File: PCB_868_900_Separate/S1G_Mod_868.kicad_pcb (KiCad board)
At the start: 4 copper layers, 60 x 33.3 mm, 79 parts, among them J2 20021121-00010C4LF, J5 0475890001-MicroUSBPort, P1 CONN_02X08, Q1 DMG2307L-7, SW1 CUS-12TB, SW2 B3U-1000P, T1 0732511150, T2 0732511150, U1 AP7361-33FGE-7, U2 ADF7023BCPZ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

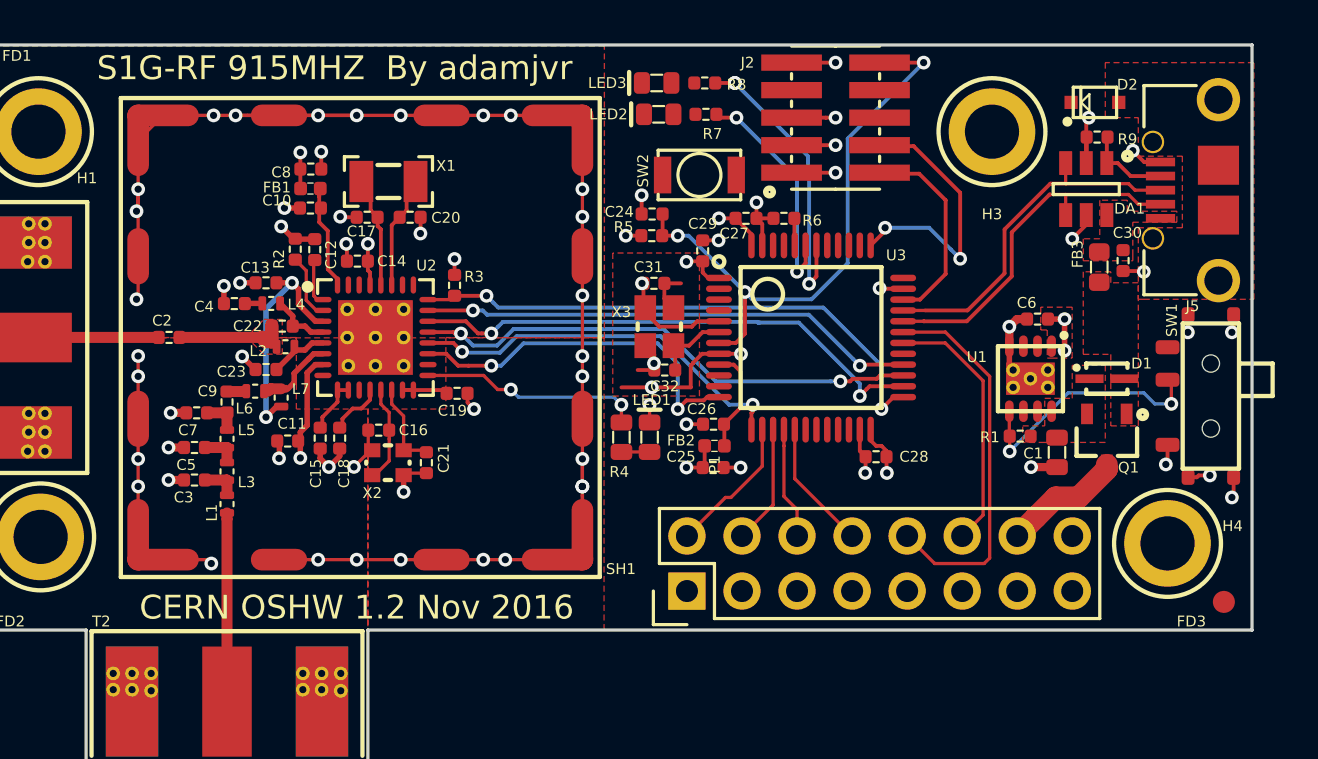
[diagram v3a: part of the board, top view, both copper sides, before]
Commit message: PCBs Tweaked A lot
PCBs have been tweaked. The separate implementation has been finished
but also has GPIOs from the MCU broken out to the connector, same for
the combined implementation. Both boards now have power indication LEDs
(red).
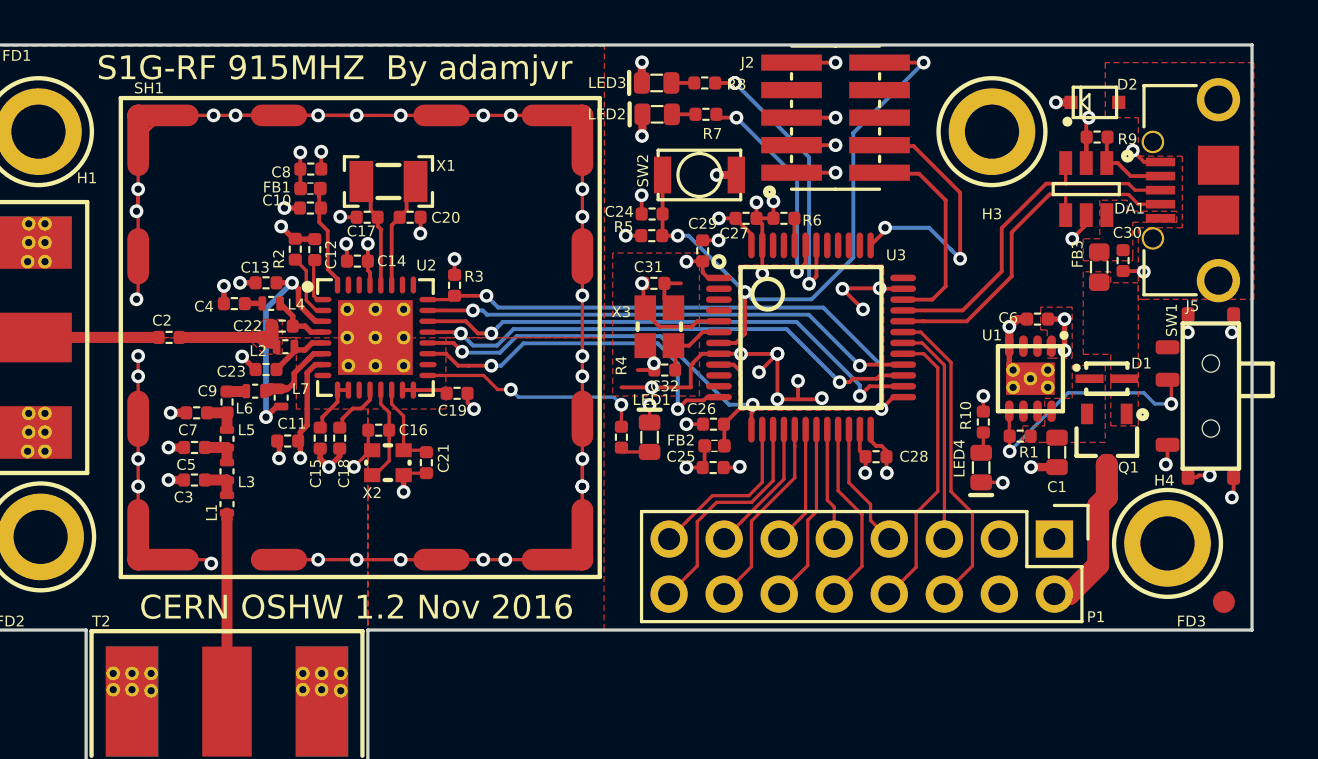
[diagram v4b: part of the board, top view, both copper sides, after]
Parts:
- added LED4: LTST-C193KRKT-5A, PCB_Footprints:LED0603, F.Cu at (104.0, 54.5)
- added R10: RC1005F102CS, PCB_Footprints:R0402, F.Cu at (104.1, 52.4)
- R4: value RC1608J202CS -> RC1005F102CS; footprint PCB_Footprints:R0603 -> PCB_Footprints:R0402
- moved P1 17.1 mm to (107.4, 57.8), turned to 270 degrees
- moved LED2 0.07 mm to (89.0, 38.2)
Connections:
- P1 pad 1: Net-(P1-Pad1) -> GND
- P1 pad 10: /MCU - STM32L052K8T6/USART1_RX -> /MCU - STM32L052K8T6/GPIO_PB10
- P1 pad 11: Net-(P1-Pad11) -> /MCU - STM32L052K8T6/GPIO_PB0
- P1 pad 12: /MCU - STM32L052K8T6/USART1_TX -> /MCU - STM32L052K8T6/GPIO_PB1
- P1 pad 13: Net-(P1-Pad13) -> /MCU - STM32L052K8T6/SPI2_MISO
- P1 pad 14: /PSU_IN -> /MCU - STM32L052K8T6/SPI2_MOSI
- P1 pad 15: GND -> /MCU - STM32L052K8T6/SPI2_NSS
- P1 pad 16: GND -> /MCU - STM32L052K8T6/SPI2_SCLK
- P1 pad 2: /MCU - STM32L052K8T6/SPI2_NSS -> /PSU_IN
- P1 pad 4: /MCU - STM32L052K8T6/SPI2_SCLK -> Net-(P1-Pad4)
- P1 pad 5: Net-(P1-Pad5) -> /MCU - STM32L052K8T6/USART1_TX
- P1 pad 6: /MCU - STM32L052K8T6/SPI2_MISO -> /MCU - STM32L052K8T6/USART1_RX
- P1 pad 7: Net-(P1-Pad7) -> /MCU - STM32L052K8T6/GPIO_PB11
- P1 pad 8: /MCU - STM32L052K8T6/SPI2_MOSI -> /MCU - STM32L052K8T6/GPIO_PA8
- P1 pad 9: Net-(P1-Pad9) -> /MCU - STM32L052K8T6/GPIO_PB2
- U3 pad 18: Net-(U3-Pad18) -> /MCU - STM32L052K8T6/GPIO_PB0
- U3 pad 19: Net-(U3-Pad19) -> /MCU - STM32L052K8T6/GPIO_PB1
- U3 pad 20: Net-(U3-Pad20) -> /MCU - STM32L052K8T6/GPIO_PB2
- U3 pad 21: Net-(U3-Pad21) -> /MCU - STM32L052K8T6/GPIO_PB10
- U3 pad 22: Net-(U3-Pad22) -> /MCU - STM32L052K8T6/GPIO_PB11
- U3 pad 29: Net-(U3-Pad29) -> /MCU - STM32L052K8T6/GPIO_PA8
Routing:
- net GND: track 141.9 -> 159.5 mm, vias 69 -> 84
- net /MCU - STM32L052K8T6/GPIO_PA8: track 0.00 -> 13.2 mm
- net /MCU - STM32L052K8T6/GPIO_PB10: track 0.00 -> 8.58 mm
- net /MCU - STM32L052K8T6/GPIO_PB1: track 0.00 -> 8.30 mm
- net /MCU - STM32L052K8T6/GPIO_PB11: track 0.00 -> 5.82 mm
- net /MCU - STM32L052K8T6/GPIO_PB0: track 0.00 -> 5.57 mm
- net /MCU - STM32L052K8T6/GPIO_PB2: track 0.00 -> 5.18 mm
- net /MCU - STM32L052K8T6/SPI2_SCLK: track 5.50 -> 10.5 mm
- net /MCU - STM32L052K8T6/USART1_RX: track 17.7 -> 14.4 mm
- net /MCU - STM32L052K8T6/SPI2_MOSI: track 6.00 -> 8.94 mm
- net /PSU_IN: track 5.61 -> 7.57 mm
- net /MCU - STM32L052K8T6/NRST: track 27.5 -> 29.3 mm
- net /MCU - STM32L052K8T6/USART1_TX: track 12.0 -> 10.4 mm
- net /MCU - STM32L052K8T6/SPI2_NSS: track 6.50 -> 7.81 mm
- net Net-(LED3-Pad1): track 0.00 -> 1.06 mm
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
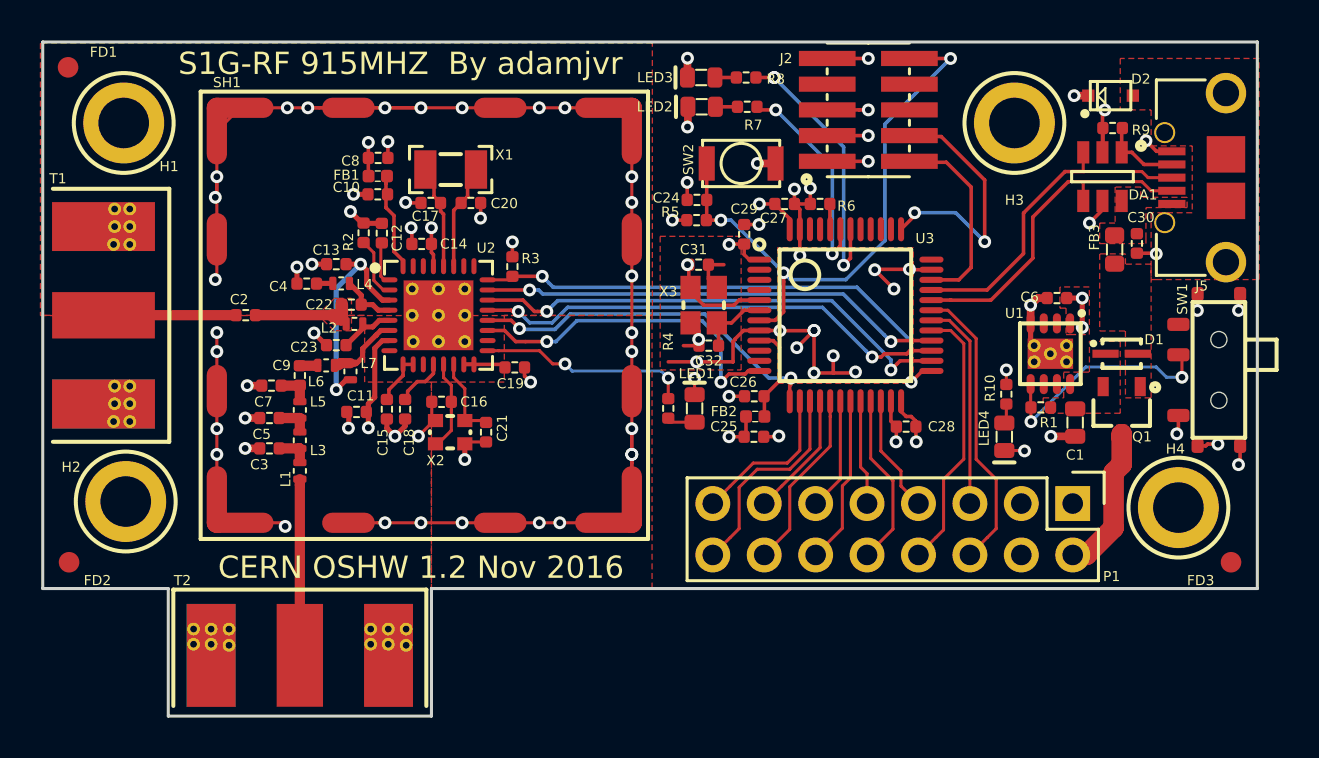
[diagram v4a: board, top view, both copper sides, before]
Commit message: Grounding and Adapter
Grounding changed on both versions of the 915MHZ/868MHZ versions of the
radio both the combined and separate antenna versions. Also an adapter
is being developed for alternative connection options.
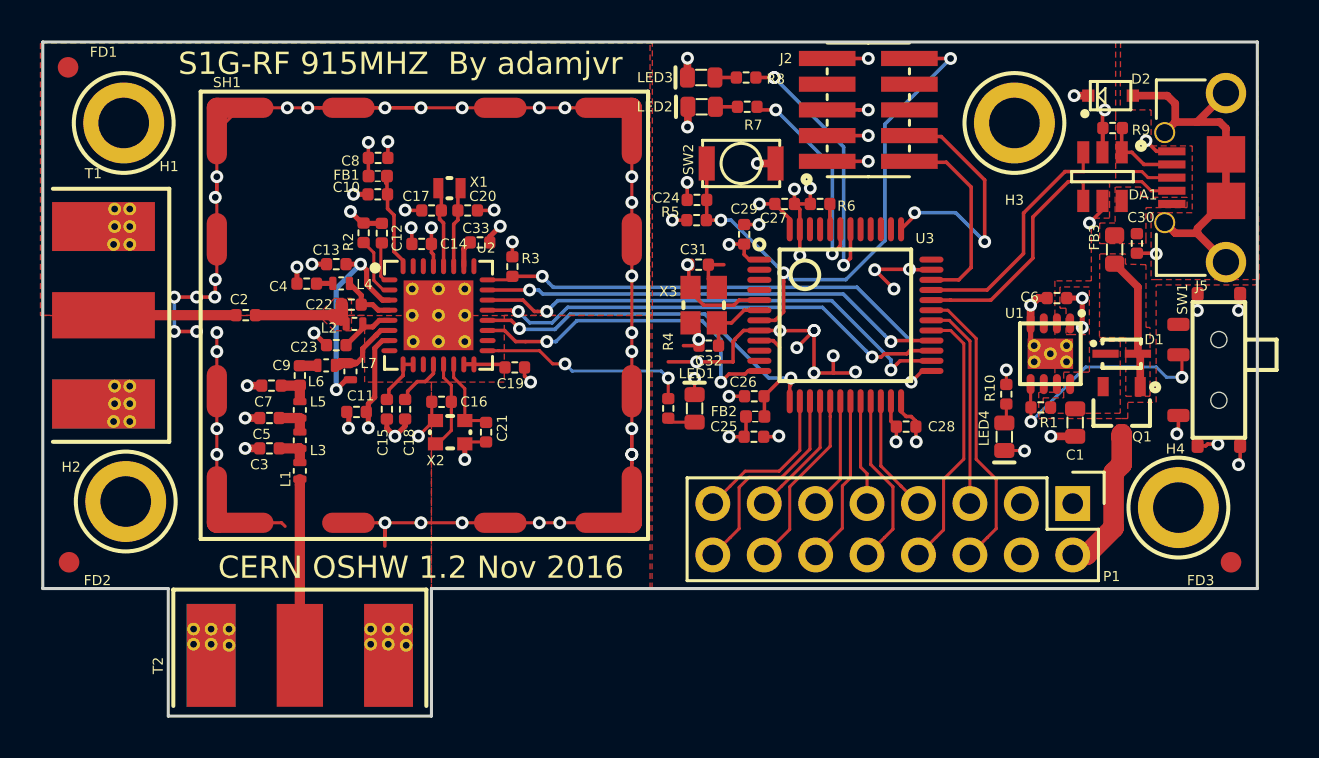
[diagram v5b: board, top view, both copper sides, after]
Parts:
- added C33: CL10B224JO8NNNC, PCB_Footprints:C0402, F.Cu at (78.1, 44.9)
- C17, C20: value CL05C180GB5NCNC -> CL05C090CB5NNNC
- X1: value ABS07-32.768KHZ-9-T -> ABS05-32.768KHZ-9-T; footprint PCB_Footprints:ABS07-32.768KHZ-9-T -> PCB_Footprints:ABS05-32.768KHZ-9-T
- moved X1 0.92 mm to (76.6, 42.2)
- moved C20 0.40 mm to (77.5, 43.3)
- moved C17 0.37 mm to (75.7, 43.3), turned to 0 degrees
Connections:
- C17 pad 1: Net-(C17-Pad1) -> GND
- C17 pad 2: GND -> Net-(C17-Pad2)
- U2 pad 28: Net-(C17-Pad1) -> Net-(C17-Pad2)
- X1 pad 1: Net-(C17-Pad1) -> Net-(C17-Pad2)
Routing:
- net Net-(D2-Pad1): track 0.00 -> 18.2 mm
- net GND: track 159.5 -> 168.3 mm, vias 84 -> 89
- net /VBUS: track 0.00 -> 6.60 mm
- net Net-(C17-Pad1): track 5.15 -> 0.00 mm
- net Net-(C17-Pad2): track 0.00 -> 4.04 mm
- net Net-(C33-Pad1): track 0.00 -> 1.31 mm
- net Net-(C20-Pad1): track 5.23 -> 4.00 mm
- added copper zone on B.Cu, net GND
- added copper zone on In2.Cu, net GND
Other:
- board text added: "S1G-RF 915MHZ Radio By adamjvr CERN OSHW 1.2 Nov 2016 Designed By Adam Vadala-Roth https://github.com/adamjvr/S1G-Mod"

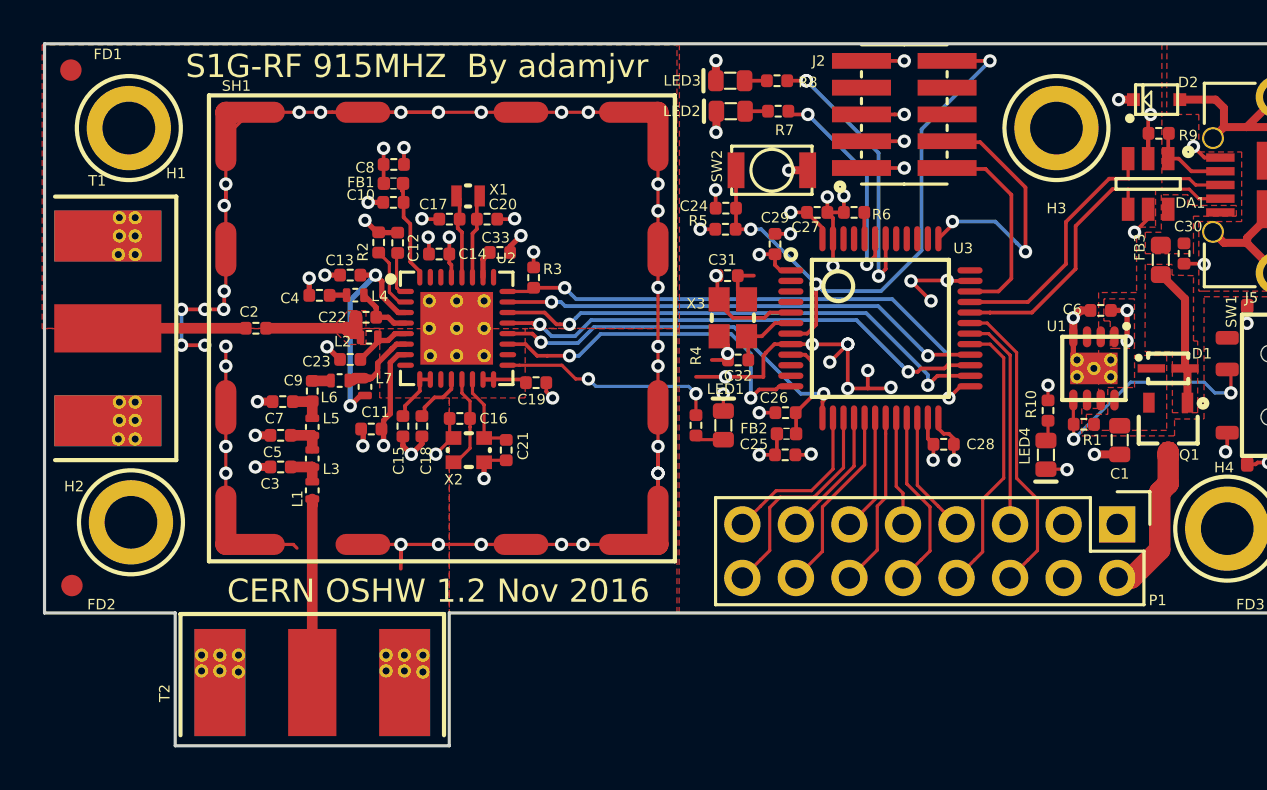
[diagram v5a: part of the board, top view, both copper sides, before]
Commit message: Separate Antenna Via Stiching
The S1G implementation with separate antennas and matching circuitry has
been thoroughly stiched with vias linking all ground pours to the
internal plane with a significant amunt of connection points.
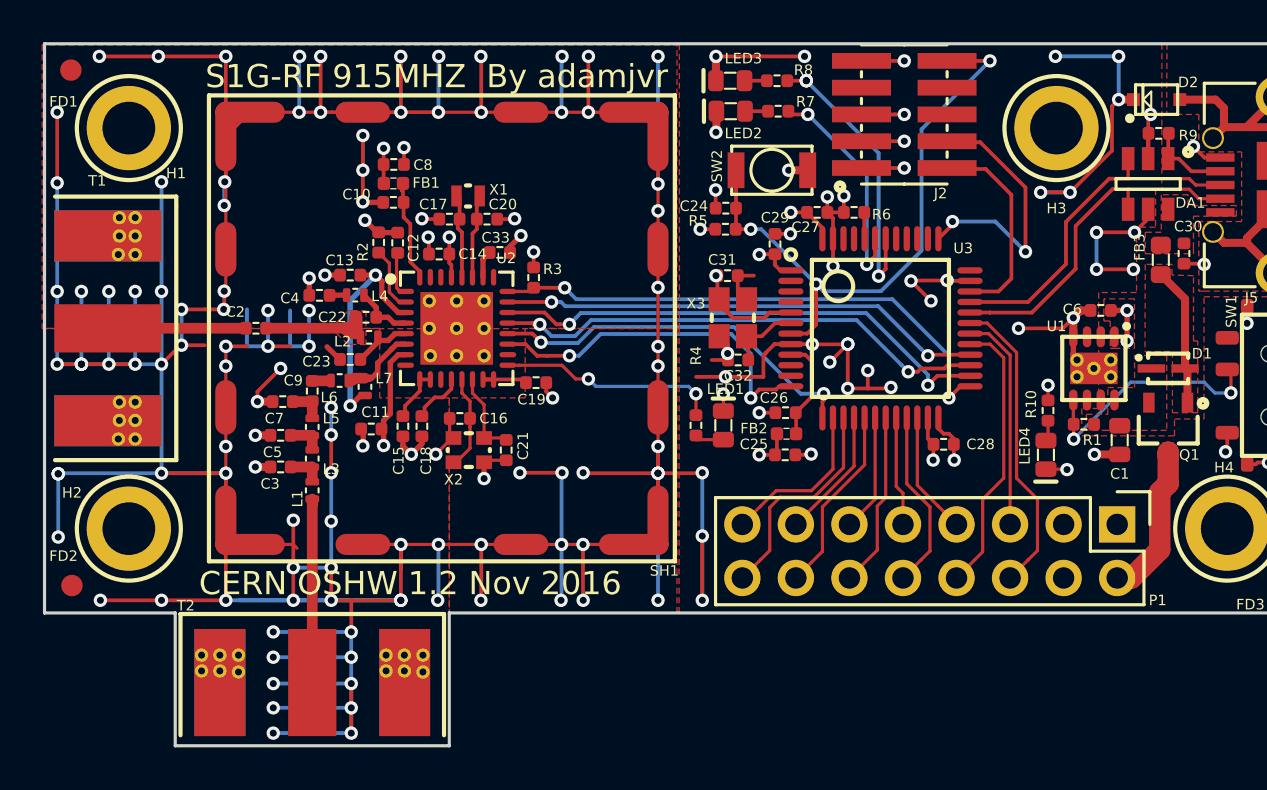
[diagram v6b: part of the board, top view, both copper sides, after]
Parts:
- moved H2 0.32 mm to (60.5, 58.0)
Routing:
- net GND: track 168.3 -> 421.4 mm, vias 89 -> 166

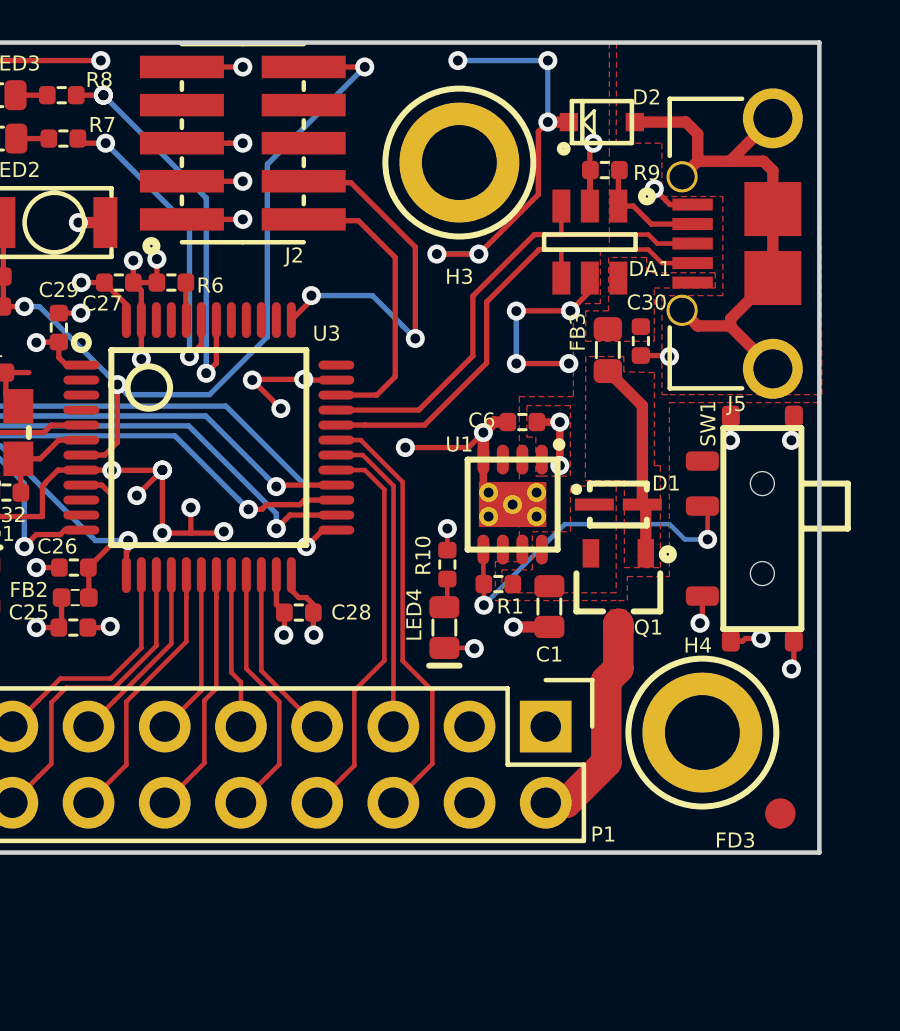
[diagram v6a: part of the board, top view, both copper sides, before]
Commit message: Additional GPIO
Two additional GPIO pins from the STM32L0 have been added to the
connector, now there is a signal on every pin. The connector component
has been replaced with one that has a STEP 3D model for proper 3D model
exporting from KiCAD for enclosure design. This has been done to both
versions of the radio.
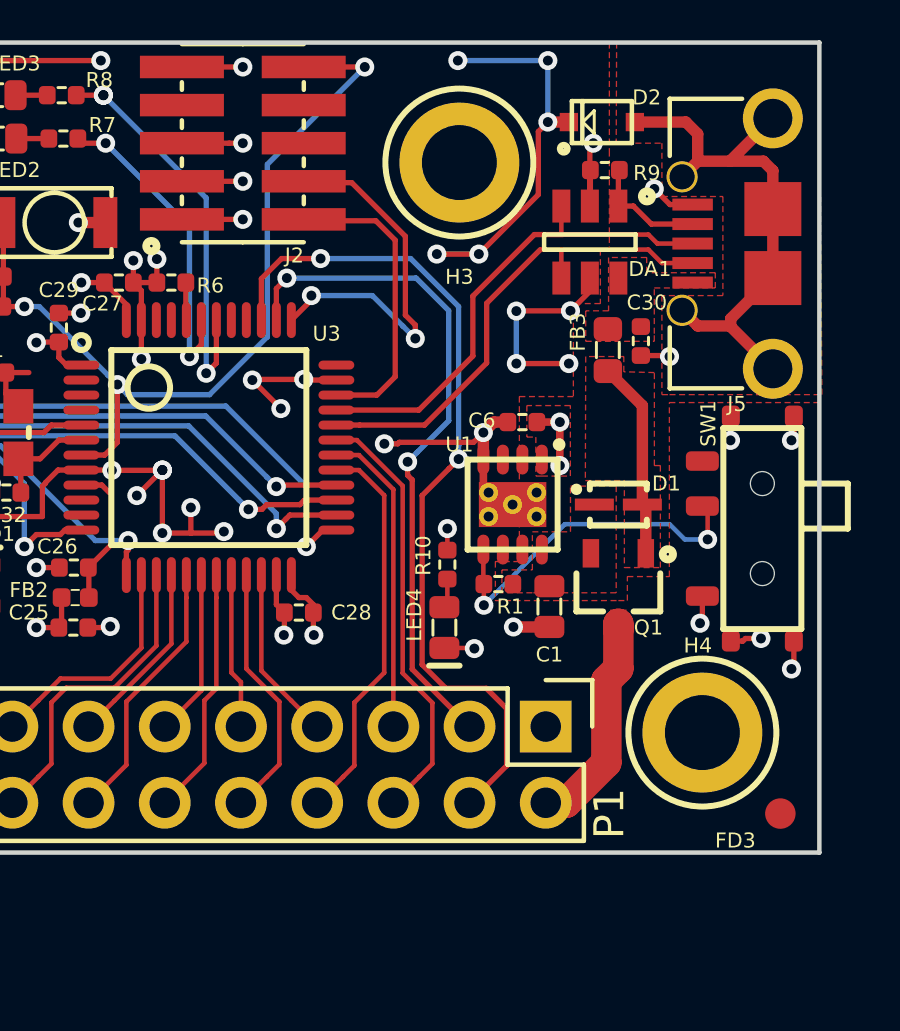
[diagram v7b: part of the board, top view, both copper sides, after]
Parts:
- P1: value CONN_02X08 -> 61301621121; footprint Pin_Headers:Pin_Header_Straight_2x08 -> PCB_Footprints:61301621121
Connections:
- P1 pad 3: Net-(P1-Pad3) -> /MCU - STM32L052K8T6/GPIO_PA15
- P1 pad 4: Net-(P1-Pad4) -> /MCU - STM32L052K8T6/GPIO_PB3
- U3 pad 38: Net-(U3-Pad38) -> /MCU - STM32L052K8T6/GPIO_PA15
- U3 pad 39: Net-(U3-Pad39) -> /MCU - STM32L052K8T6/GPIO_PB3
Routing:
- net /MCU - STM32L052K8T6/GPIO_PB3: track 0.00 -> 28.4 mm, vias 0 -> 2
- net /MCU - STM32L052K8T6/GPIO_PA15: track 0.00 -> 22.7 mm, vias 0 -> 2
- net (no net): track 0.00 -> 9.83 mm, vias 1 -> 5
- net GND: track 421.4 -> 412.2 mm, vias 166 -> 162
